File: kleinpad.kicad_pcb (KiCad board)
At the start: 2 copper layers, 79 x 79 mm, 31 parts, among them J1 Conn_01x02, J2 Conn_01x05, SW1 SW_Push, SW2 RotaryEncoder_Switch, U1 SuperMini nRF52840

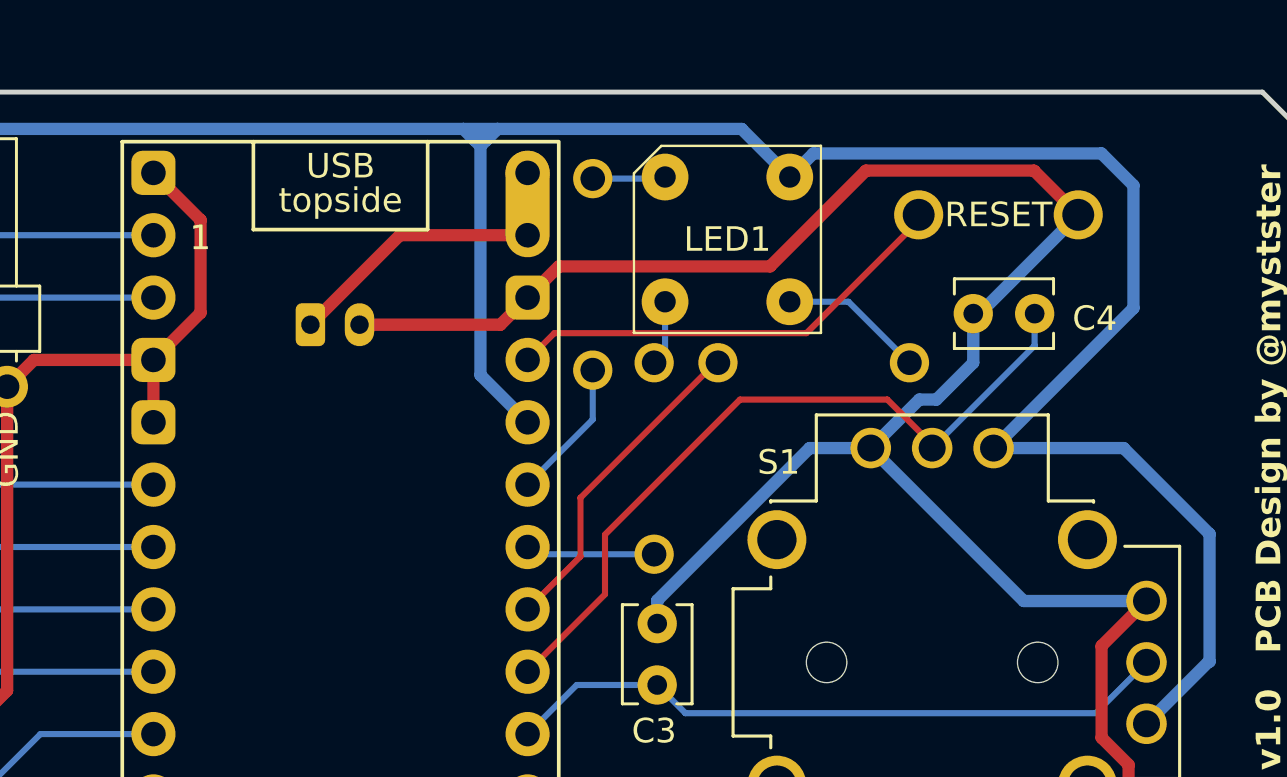
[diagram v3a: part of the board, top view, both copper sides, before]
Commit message: fix: 抵抗周りの配線のレイアウトを変更
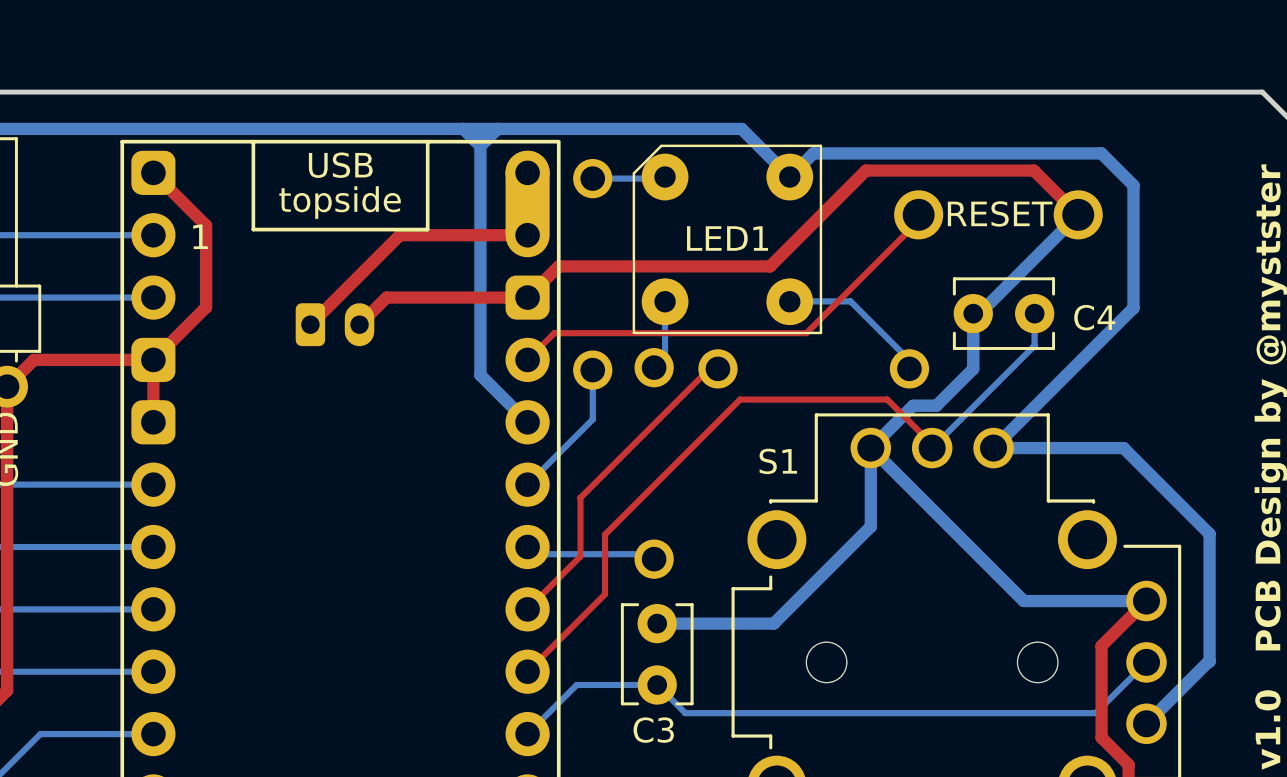
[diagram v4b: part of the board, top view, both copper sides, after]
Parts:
- moved R3 0.25 mm to (160.0, 71.8)
- moved R2 0.20 mm to (153.5, 75.6)
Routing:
- net GND: track 171.9 -> 173.5 mm
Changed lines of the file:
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@@
 	(footprint "Keebio-Parts.pretty-master:Resistor-Compact-1-side"
 		(layer "B.Cu")
-		(at 153.5 75.4 -90)
+		(at 153.5 75.6 -90)
 		(property "Reference" "R2"
 			(at 0 -1.5 270)
@@
 	(footprint "Keebio-Parts.pretty-master:Resistor-Compact-1-side"
 		(layer "B.Cu")
-		(at 160 71.5 180)
+		(at 160 71.75 180)
 		(property "Reference" "R3"
 			(at 0 -1.5 0)
@@
 	)
 	(segment
+		(start 142.6045 68.8455)
+		(end 141.5 69.95)
+		(width 0.5)
+		(layer "F.Cu")
+		(net 2)
+	)
+	(segment
 		(start 133.105625 71.3855)
 		(end 133.105625 73.9255)
@@
 	)
 	(segment
-		(start 141.5 69.95)
-		(end 147.241125 69.95)
+		(start 148.345625 68.8455)
+		(end 142.6045 68.8455)
 		(width 0.5)
 		(layer "F.Cu")
@@
 	)
 	(segment
-		(start 149.615625 67.5755)
-		(end 158.225625 67.5755)
+		(start 135.25 69.241125)
+		(end 133.105625 71.3855)
 		(width 0.5)
 		(layer "F.Cu")
@@
 	)
 	(segment
-		(start 133.105625 71.3855)
-		(end 135.025625 69.4655)
+		(start 149.615625 67.5755)
+		(end 158.225625 67.5755)
 		(width 0.5)
 		(layer "F.Cu")
@@
 	)
 	(segment
-		(start 147.241125 69.95)
-		(end 148.345625 68.8455)
-		(width 0.5)
-		(layer "F.Cu")
-		(net 2)
-	)
-	(segment
 		(start 148.345625 68.8455)
 		(end 149.615625 67.5755)
@@
 	)
 	(segment
-		(start 135.025625 69.4655)
-		(end 135.025625 65.6855)
+		(start 135.25 65.909875)
+		(end 135.25 69.241125)
 		(width 0.5)
 		(layer "F.Cu")
@@
 	)
 	(segment
+		(start 133.105625 63.7655)
+		(end 135.25 65.909875)
+		(width 0.5)
+		(layer "F.Cu")
+		(net 2)
+	)
+	(segment
 		(start 161.575625 93.9555)
 		(end 163.295625 95.6755)
@@
 	)
 	(segment
-		(start 135.025625 65.6855)
-		(end 133.105625 63.7655)
-		(width 0.5)
-		(layer "F.Cu")
-		(net 2)
-	)
-	(segment
 		(start 128.235625 71.3855)
 		(end 127.145625 72.4755)
@@
 	)
 	(segment
-		(start 153.625625 82.1255)
-		(end 153.625625 81.184252)
-		(width 0.5)
-		(layer "B.Cu")
-		(net 2)
-	)
-	(segment
 		(start 105.775625 84.7255)
 		(end 105.775625 89.1755)
@@
 	)
 	(segment
-		(start 166.5 71.5)
-		(end 165 73)
+		(start 162.325625 78.174375)
+		(end 158.3745 82.1255)
 		(width 0.5)
 		(layer "B.Cu")
@@
 	)
 	(segment
-		(start 164.301125 73)
+		(start 168.555625 81.2055)
 		(end 162.325625 74.9755)
 		(width 0.5)
@@
 	)
 	(segment
-		(start 153.625625 81.184252)
-		(end 159.834377 74.9755)
+		(start 166.5 71.75)
+		(end 165 73.25)
 		(width 0.5)
 		(layer "B.Cu")
@@
 	)
 	(segment
-		(start 168.555625 81.2055)
-		(end 162.325625 74.9755)
+		(start 158.3745 82.1255)
+		(end 153.625625 82.1255)
 		(width 0.5)
 		(layer "B.Cu")
@@
 	)
 	(segment
-		(start 159.834377 74.9755)
+		(start 164.051125 73.25)
 		(end 162.325625 74.9755)
 		(width 0.5)
@@
 	)
 	(segment
+		(start 162.325625 74.9755)
+		(end 162.325625 78.174375)
+		(width 0.5)
+		(layer "B.Cu")
+		(net 2)
+	)
+	(segment
+		(start 165 73.25)
+		(end 164.051125 73.25)
+		(width 0.5)
+		(layer "B.Cu")
+		(net 2)
+	)
+	(segment
 		(start 166.5 69.5)
-		(end 166.5 71.5)
+		(end 166.5 71.75)
 		(width 0.5)
 		(layer "B.Cu")
@@
 	)
 	(segment
-		(start 165 73)
-		(end 164.301125 73)
-		(width 0.5)
-		(layer "B.Cu")
-		(net 2)
-	)
-	(segment
 		(start 105.775625 89.1755)
 		(end 105.825625 89.2255)
@@
 	)
 	(segment
+		(start 159.986625 62.9745)
+		(end 171.724625 62.9745)
+		(width 0.5)
+		(layer "B.Cu")
+		(net 19)
+	)
+	(segment
 		(start 146.675625 62.4255)
 		(end 146.686625 62.4145)
@@
 	)
 	(segment
-		(start 173.025625 69.2755)
+		(start 171.724625 62.9745)
 		(end 173.025625 64.2755)
 		(width 0.5)
@@
 	)
 	(segment
+		(start 173.025625 69.2755)
+		(end 167.325625 74.9755)
+		(width 0.5)
+		(layer "B.Cu")
+		(net 19)
+	)
+	(segment
 		(start 146.164625 62.4145)
 		(end 146.425625 62.6755)
@@
 	)
 	(segment
-		(start 146.425625 62.6755)
-		(end 146.686625 62.4145)
+		(start 159.025625 63.9355)
+		(end 159.986625 62.9745)
 		(width 0.5)
 		(layer "B.Cu")
@@
 	)
 	(segment
-		(start 176.125625 78.4755)
-		(end 172.625625 74.9755)
+		(start 173.025625 64.2755)
+		(end 173.025625 69.2755)
 		(width 0.5)
 		(layer "B.Cu")
@@
 	)
 	(segment
-		(start 171.724625 62.9745)
-		(end 159.986625 62.9745)
+		(start 146.425625 62.6755)
+		(end 146.686625 62.4145)
+		(width 0.5)
+		(layer "B.Cu")
+		(net 19)
+	)
+	(segment
+		(start 176.125625 78.4755)
+		(end 172.625625 74.9755)
 		(width 0.5)
 		(layer "B.Cu")
@@
 	)
 	(segment
-		(start 167.325625 74.9755)
-		(end 173.025625 69.2755)
-		(width 0.5)
-		(layer "B.Cu")
-		(net 19)
-	)
-	(segment
 		(start 172.625625 74.9755)
 		(end 167.325625 74.9755)
@@
 	)
 	(segment
-		(start 173.025625 64.2755)
-		(end 171.724625 62.9745)
-		(width 0.5)
-		(layer "B.Cu")
-		(net 19)
-	)
-	(segment
-		(start 159.986625 62.9745)
-		(end 159.025625 63.9355)
-		(width 0.5)
-		(layer "B.Cu")
-		(net 19)
-	)
-	(segment
 		(start 109.625625 61.9755)
 		(end 145.725625 61.9755)
@@
 	)
 	(segment
-		(start 161.4155 69.0155)
-		(end 163.9 71.5)
+		(start 161.5 69)
+		(end 163.9 71.4)
+		(width 0.25)
+		(layer "B.Cu")
+		(net 40)
+	)
+	(segment
+		(start 163.9 71.4)
+		(end 163.9 71.75)
+		(width 0.25)
+		(layer "B.Cu")
+		(net 40)
+	)
+	(segment
+		(start 159.2345 69.0155)
+		(end 159.25 69)
+		(width 0.25)
+		(layer "B.Cu")
+		(net 40)
+	)
+	(segment
+		(start 159.25 69)
+		(end 161.5 69)
 		(width 0.25)
 		(layer "B.Cu")
@@
 	(segment
 		(start 159.025625 69.0155)
-		(end 161.4155 69.0155)
+		(end 159.2345 69.0155)
 		(width 0.25)
 		(layer "B.Cu")

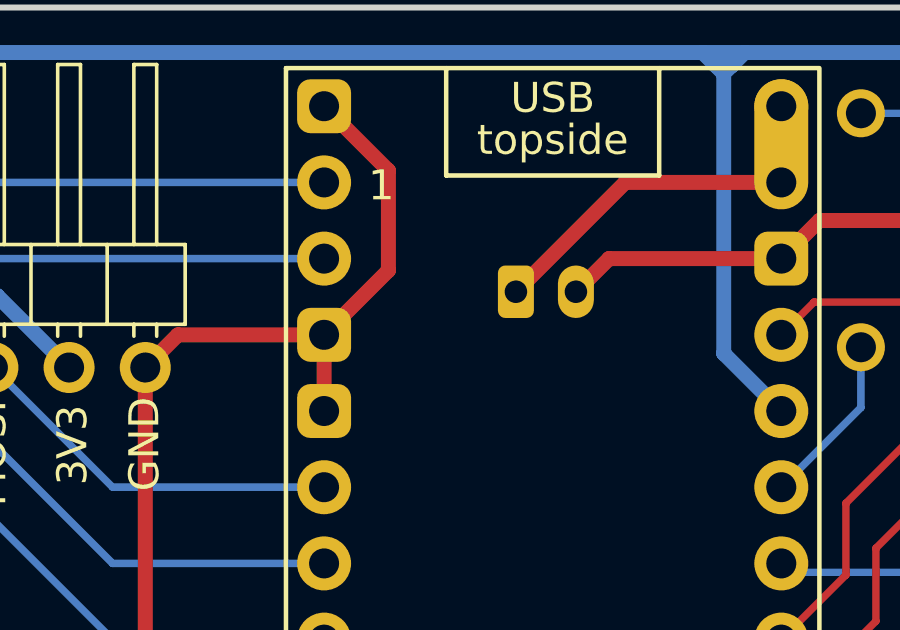
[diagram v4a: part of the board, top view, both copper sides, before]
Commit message: fix: 未接続の配線を接続
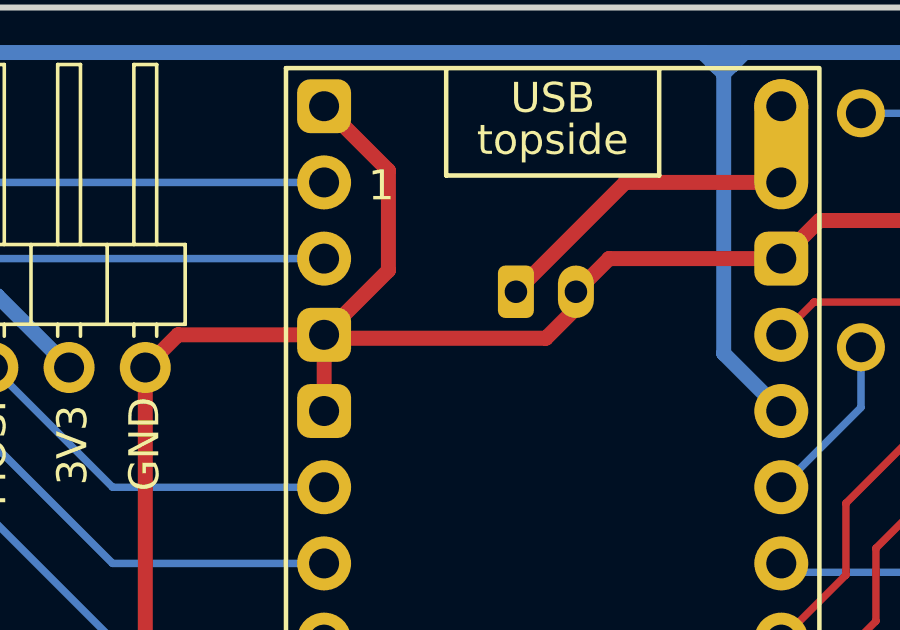
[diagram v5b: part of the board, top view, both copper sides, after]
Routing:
- net GND: track 173.5 -> 182.9 mm
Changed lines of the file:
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@@
+	)
+	(segment
+		(start 141.5 70.5)
+		(end 141.5 69.95)
+		(width 0.5)
+		(layer "F.Cu")
+		(net 2)
+	)
+	(segment
+		(start 140.5 71.5)
+		(end 141.5 70.5)
+		(width 0.5)
+		(layer "F.Cu")
+		(net 2)
 	)
 	(segment
@@
 	)
 	(segment
+		(start 133.105625 71.3855)
+		(end 133.220125 71.5)
+		(width 0.5)
+		(layer "F.Cu")
+		(net 2)
+	)
+	(segment
 		(start 149.615625 67.5755)
 		(end 158.225625 67.5755)
 		(width 0.5)
 		(layer "F.Cu")
+		(net 2)
+	)
+	(segment
+		(start 133.220125 71.5)
+		(end 140.5 71.5)
+		(width 0.5)
+		(layer "F.Cu")

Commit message: feat: bump version
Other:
- board text added: "Kleinpad v1.1 PCB Design by @mystster"
- board text removed: "Kleinpad v1.0 PCB Design by @mystster"
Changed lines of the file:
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@@
 		)
 	)
-	(gr_text "Kleinpad v1.0   PCB Design by @mystster"
+	(gr_text "Kleinpad v1.1   PCB Design by @mystster"
 		(at 179.125625 95.3755 90)
 		(layer "F.SilkS")

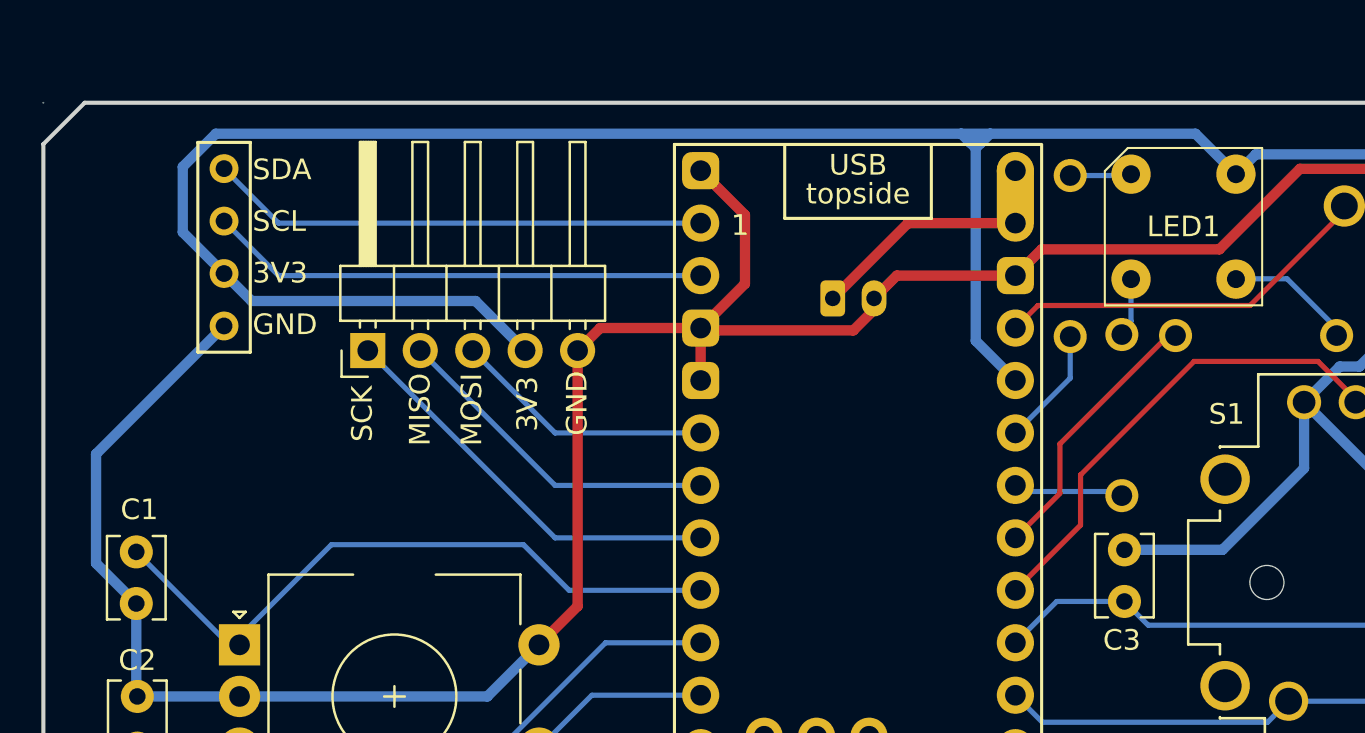
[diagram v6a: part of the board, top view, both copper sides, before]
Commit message: fix: OLEDとSuperMiniの干渉 Fixes #4
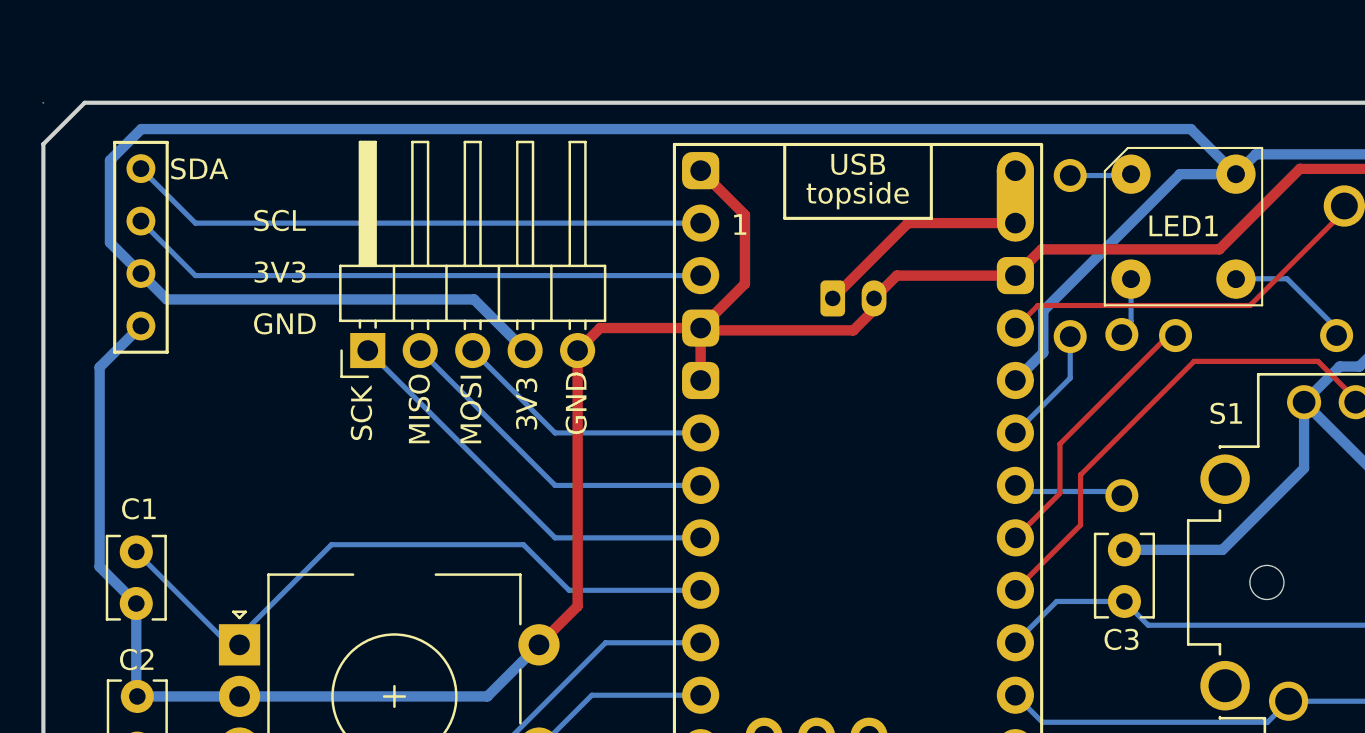
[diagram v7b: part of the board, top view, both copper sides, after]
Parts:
- moved OL1 4.03 mm to (106.0, 63.7)
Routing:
- net 3V3: track 136.2 -> 145.4 mm
- net SDA: track 24.2 -> 28.2 mm
- net SCL: track 24.2 -> 28.2 mm
- net GND: track 182.9 -> 181.1 mm
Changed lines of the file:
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@@
 	(footprint "kbd_Parts:OLED"
 		(layer "F.Cu")
-		(at 110.025625 63.6655 -90)
+		(at 106 63.6655 -90)
 		(descr "Connecteur 6 pins")
 		(tags "CONN DEV")
@@
 	)
 	(gr_text "SDA"
-		(at 111.4 64.3 0)
+		(at 107.374375 64.3 0)
 		(layer "F.SilkS")
 		(effects
@@
 	)
 	(segment
-		(start 103.825625 77.4855)
-		(end 103.825625 82.7755)
+		(start 104 73.2855)
+		(end 104 82.949875)
 		(width 0.5)
 		(layer "B.Cu")
@@
 	)
 	(segment
+		(start 104 82.949875)
+		(end 105.775625 84.7255)
+		(width 0.5)
+		(layer "B.Cu")
+		(net 2)
+	)
+	(segment
 		(start 158.3745 82.1255)
 		(end 153.625625 82.1255)
@@
 	)
 	(segment
+		(start 106 71.2855)
+		(end 104 73.2855)
+		(width 0.5)
+		(layer "B.Cu")
+		(net 2)
+	)
+	(segment
 		(start 173.555625 81.2055)
 		(end 168.555625 81.2055)
@@
 	)
 	(segment
-		(start 110.025625 71.2855)
-		(end 103.825625 77.4855)
-		(width 0.5)
-		(layer "B.Cu")
-		(net 2)
-	)
-	(segment
-		(start 103.825625 82.7755)
-		(end 105.775625 84.7255)
-		(width 0.5)
-		(layer "B.Cu")
-		(net 2)
-	)
-	(segment
 		(start 105.775625 89.1755)
 		(end 105.825625 89.2255)
@@
 	)
 	(segment
-		(start 145.725625 61.9755)
-		(end 147.125625 61.9755)
-		(width 0.5)
-		(layer "B.Cu")
-		(net 19)
-	)
-	(segment
 		(start 159.986625 62.9745)
 		(end 171.724625 62.9745)
@@
 	)
 	(segment
-		(start 146.675625 62.4255)
-		(end 146.686625 62.4145)
+		(start 156.840125 61.75)
+		(end 159.025625 63.9355)
 		(width 0.5)
 		(layer "B.Cu")
@@
 	)
 	(segment
-		(start 171.724625 62.9745)
-		(end 173.025625 64.2755)
+		(start 107.2545 70)
+		(end 122.130125 70)
 		(width 0.5)
 		(layer "B.Cu")
@@
 	)
 	(segment
-		(start 146.425625 72.0055)
-		(end 146.425625 62.6755)
+		(start 171.724625 62.9745)
+		(end 173.025625 64.2755)
 		(width 0.5)
 		(layer "B.Cu")
@@
 	)
 	(segment
-		(start 108.025625 66.7455)
-		(end 108.025625 63.5755)
+		(start 149.696625 72.5745)
+		(end 149.696625 70.553375)
 		(width 0.5)
 		(layer "B.Cu")
@@
 	)
 	(segment
-		(start 146.164625 62.4145)
-		(end 146.425625 62.6755)
+		(start 149.696625 70.553375)
+		(end 156.3145 63.9355)
 		(width 0.5)
 		(layer "B.Cu")
@@
 	)
 	(segment
-		(start 146.425625 62.6755)
-		(end 146.686625 62.4145)
+		(start 106 68.7455)
+		(end 107.2545 70)
 		(width 0.5)
 		(layer "B.Cu")
@@
 	)
 	(segment
-		(start 176.125625 78.4755)
-		(end 172.625625 74.9755)
+		(start 104.5 63.269931)
+		(end 106.019931 61.75)
 		(width 0.5)
 		(layer "B.Cu")
@@
 	)
 	(segment
-		(start 148.345625 73.9255)
-		(end 146.425625 72.0055)
+		(start 176.125625 78.4755)
+		(end 172.625625 74.9755)
 		(width 0.5)
 		(layer "B.Cu")
@@
 	)
 	(segment
-		(start 145.725625 61.9755)
-		(end 146.164625 62.4145)
+		(start 106.019931 61.75)
+		(end 156.840125 61.75)
 		(width 0.5)
 		(layer "B.Cu")
@@
 	)
 	(segment
-		(start 110.025625 68.7455)
-		(end 108.025625 66.7455)
+		(start 106 68.7455)
+		(end 104.5 67.2455)
 		(width 0.5)
 		(layer "B.Cu")
@@
 	)
 	(segment
-		(start 176.125625 83.6755)
-		(end 176.125625 78.4755)
+		(start 104.5 67.2455)
+		(end 104.5 63.269931)
 		(width 0.5)
 		(layer "B.Cu")
@@
 	)
 	(segment
-		(start 157.065625 61.9755)
-		(end 159.025625 63.9355)
+		(start 122.130125 70)
+		(end 124.605625 72.4755)
 		(width 0.5)
 		(layer "B.Cu")
@@
 	)
 	(segment
-		(start 146.175625 62.4255)
-		(end 146.675625 62.4255)
-		(width 0.5)
-		(layer "B.Cu")
-		(net 19)
-	)
-	(segment
-		(start 108.025625 63.5755)
-		(end 109.625625 61.9755)
+		(start 176.125625 83.6755)
+		(end 176.125625 78.4755)
 		(width 0.5)
 		(layer "B.Cu")
@@
 	)
 	(segment
-		(start 109.625625 61.9755)
-		(end 145.725625 61.9755)
+		(start 148.345625 73.9255)
+		(end 149.696625 72.5745)
 		(width 0.5)
 		(layer "B.Cu")
@@
 	)
 	(segment
-		(start 146.686625 62.4145)
-		(end 147.125625 61.9755)
+		(start 156.3145 63.9355)
+		(end 159.025625 63.9355)
 		(width 0.5)
 		(layer "B.Cu")
@@
 	)
 	(segment
-		(start 122.205625 70.0755)
-		(end 111.355625 70.0755)
-		(width 0.5)
-		(layer "B.Cu")
-		(net 19)
-	)
-	(segment
-		(start 147.125625 61.9755)
-		(end 157.065625 61.9755)
-		(width 0.5)
-		(layer "B.Cu")
-		(net 19)
-	)
-	(segment
-		(start 111.355625 70.0755)
-		(end 110.025625 68.7455)
-		(width 0.5)
-		(layer "B.Cu")
-		(net 19)
-	)
-	(segment
-		(start 124.605625 72.4755)
-		(end 122.205625 70.0755)
-		(width 0.5)
-		(layer "B.Cu")
-		(net 19)
-	)
-	(segment
 		(start 126.055625 79.0055)
 		(end 133.105625 79.0055)
@@
 	)
 	(segment
-		(start 112.665625 68.8455)
-		(end 110.025625 66.2055)
+		(start 108.64 68.8455)
+		(end 106 66.2055)
 		(width 0.25)
 		(layer "B.Cu")
@@
 	(segment
 		(start 133.105625 68.8455)
-		(end 112.665625 68.8455)
+		(end 108.64 68.8455)
 		(width 0.25)
 		(layer "B.Cu")
@@
 	(segment
 		(start 133.105625 66.3055)
-		(end 112.665625 66.3055)
+		(end 108.64 66.3055)
 		(width 0.25)
 		(layer "B.Cu")
@@
 	)
 	(segment
-		(start 112.665625 66.3055)
-		(end 110.025625 63.6655)
+		(start 108.64 66.3055)
+		(end 106 63.6655)
 		(width 0.25)
 		(layer "B.Cu")
